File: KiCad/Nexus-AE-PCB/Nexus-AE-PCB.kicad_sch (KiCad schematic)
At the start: 0 parts

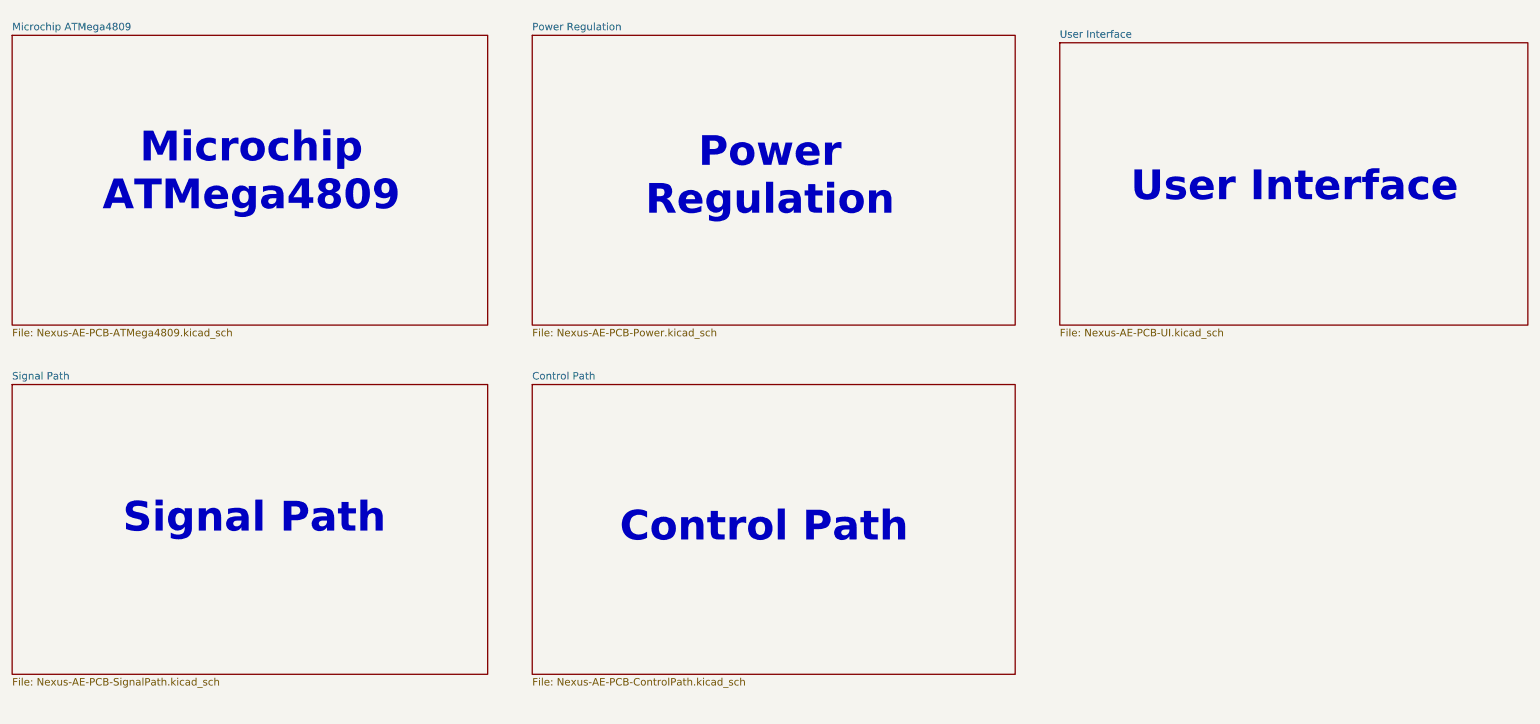
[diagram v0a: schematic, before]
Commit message: PCB and schmeatic are both approx 90% complete
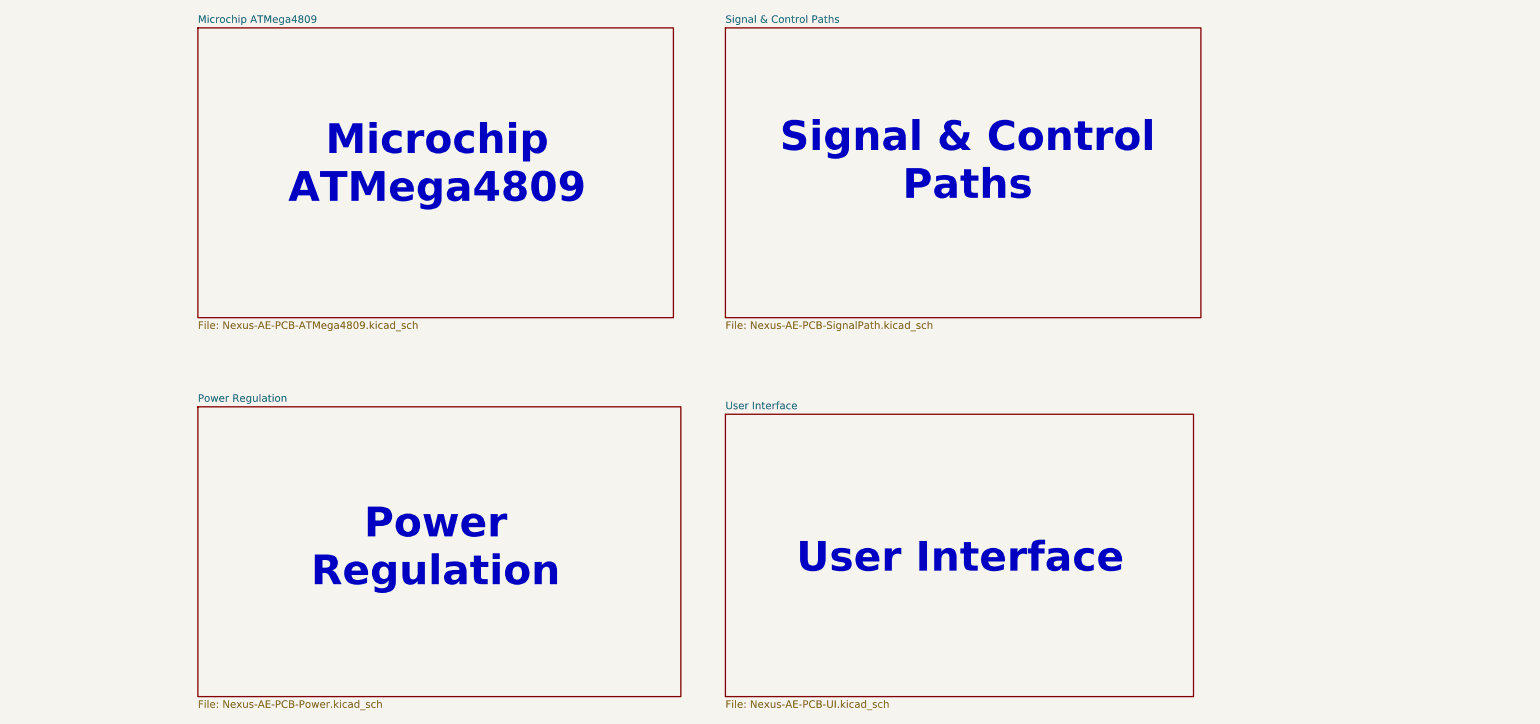
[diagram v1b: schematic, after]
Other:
- sheet Signal Path renamed Signal & Control Paths
- removed sheet Control Path
- note added: "Signal & Control Paths"
- note removed: "Control Path"
- note removed: "Signal Path"
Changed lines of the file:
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@@
 		(comment 1 "Charles H. Leggett")
 	)
-	(text "Control Path"
-		(exclude_from_sim no)
-		(at 148.844 119.634 0)
-		(effects
-			(font
-				(size 5.08 5.08)
-				(thickness 1.016)
-				(bold yes)
-			)
-		)
-	)
 	(text "User Interface"
 		(exclude_from_sim no)
-		(at 239.522 61.468 0)
-		(effects
-			(font
-				(size 5.08 5.08)
-				(thickness 1.016)
-				(bold yes)
-			)
-		)
-	)
-	(text "Signal Path"
-		(exclude_from_sim no)
-		(at 61.722 118.11 0)
+		(at 182.372 124.968 0)
+		(effects
+			(font
+				(size 5.08 5.08)
+				(thickness 1.016)
+				(bold yes)
+			)
+		)
+	)
+	(text "Signal & Control\nPaths"
+		(exclude_from_sim no)
+		(at 183.642 57.15 0)
 		(effects
 			(font
@@
 	(text "Power\nRegulation\n"
 		(exclude_from_sim no)
-		(at 149.86 59.69 0)
+		(at 92.71 123.19 0)
 		(effects
 			(font
@@
 	(text "Microchip\nATMega4809"
 		(exclude_from_sim no)
-		(at 61.214 58.928 0)
-		(effects
-			(font
-				(size 5.08 5.08)
-				(thickness 1.016)
-				(bold yes)
-			)
-		)
-	)
-	(sheet
-		(at 199.39 36.83)
+		(at 92.964 57.658 0)
+		(effects
+			(font
+				(size 5.08 5.08)
+				(thickness 1.016)
+				(bold yes)
+			)
+		)
+	)
+	(sheet
+		(at 142.24 100.33)
 		(size 80.01 48.26)
 		(exclude_from_sim no)
@@
 		)
 		(property "Sheetname" "User Interface"
-			(at 199.39 36.1184 0)
+			(at 142.24 99.6184 0)
 			(show_name no)
 			(do_not_autoplace no)
@@
 		)
 		(property "Sheetfile" "Nexus-AE-PCB-UI.kicad_sch"
-			(at 199.39 85.6746 0)
+			(at 142.24 149.1746 0)
 			(show_name no)
 			(do_not_autoplace no)
@@
 	)
 	(sheet
-		(at 109.22 95.25)
+		(at 52.07 99.06)
 		(size 82.55 49.53)
 		(exclude_from_sim no)
@@
 			(color 0 0 0 0)
 		)
-		(property "Sheetname" "Control Path"
-			(at 109.22 94.5384 0)
-			(show_name no)
-			(do_not_autoplace no)
-			(effects
-				(font
-					(size 1.27 1.27)
-				)
-				(justify left bottom)
-			)
-		)
-		(property "Sheetfile" "Nexus-AE-PCB-ControlPath.kicad_sch"
-			(at 109.22 145.3646 0)
-			(show_name no)
-			(do_not_autoplace no)
-			(effects
-				(font
-					(size 1.27 1.27)
-				)
-				(justify left top)
-			)
-		)
-		(instances
-			(project "Nexus-AE-PCB"
-				(path "/b249adcd-2848-4e56-9615-c4f1b6083abe"
-					(page "6")
-				)
-			)
-		)
-	)
-	(sheet
-		(at 109.22 35.56)
-		(size 82.55 49.53)
-		(exclude_from_sim no)
-		(in_bom yes)
-		(on_board yes)
-		(dnp no)
-		(fields_autoplaced yes)
-		(stroke
-			(width 0.1524)
-			(type solid)
-		)
-		(fill
-			(color 0 0 0 0)
-		)
 		(property "Sheetname" "Power Regulation"
-			(at 109.22 34.8484 0)
+			(at 52.07 98.3484 0)
 			(show_name no)
 			(do_not_autoplace no)
@@
 		)
 		(property "Sheetfile" "Nexus-AE-PCB-Power.kicad_sch"
-			(at 109.22 85.6746 0)
+			(at 52.07 149.1746 0)
 			(show_name no)
 			(do_not_autoplace no)
@@
 	)
 	(sheet
-		(at 20.32 95.25)
+		(at 142.24 34.29)
 		(size 81.28 49.53)
 		(exclude_from_sim no)
@@
 			(color 0 0 0 0)
 		)
-		(property "Sheetname" "Signal Path"
-			(at 20.32 94.5384 0)
+		(property "Sheetname" "Signal & Control Paths"
+			(at 142.24 33.5784 0)
 			(show_name no)
 			(do_not_autoplace no)
@@
 		)
 		(property "Sheetfile" "Nexus-AE-PCB-SignalPath.kicad_sch"
-			(at 20.32 145.3646 0)
+			(at 142.24 84.4046 0)
 			(show_name no)
 			(do_not_autoplace no)
@@
 	)
 	(sheet
-		(at 20.32 35.56)
+		(at 52.07 34.29)
 		(size 81.28 49.53)
 		(exclude_from_sim no)
@@
 		)
 		(property "Sheetname" "Microchip ATMega4809"
-			(at 20.32 34.8484 0)
+			(at 52.07 33.5784 0)
 			(show_name no)
 			(do_not_autoplace no)
@@
 		)
 		(property "Sheetfile" "Nexus-AE-PCB-ATMega4809.kicad_sch"
-			(at 20.32 85.6746 0)
-			(show_name no)
-			(do_not_autoplace no)
+			(at 52.07 84.4046 0)
+			(show_name no)
+			(do_not_autoplace no)
